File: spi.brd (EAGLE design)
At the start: 40.3 x 33 mm, 7 parts, among them IC2 25AA080SN, IC3 25AA080P, X1 2510-

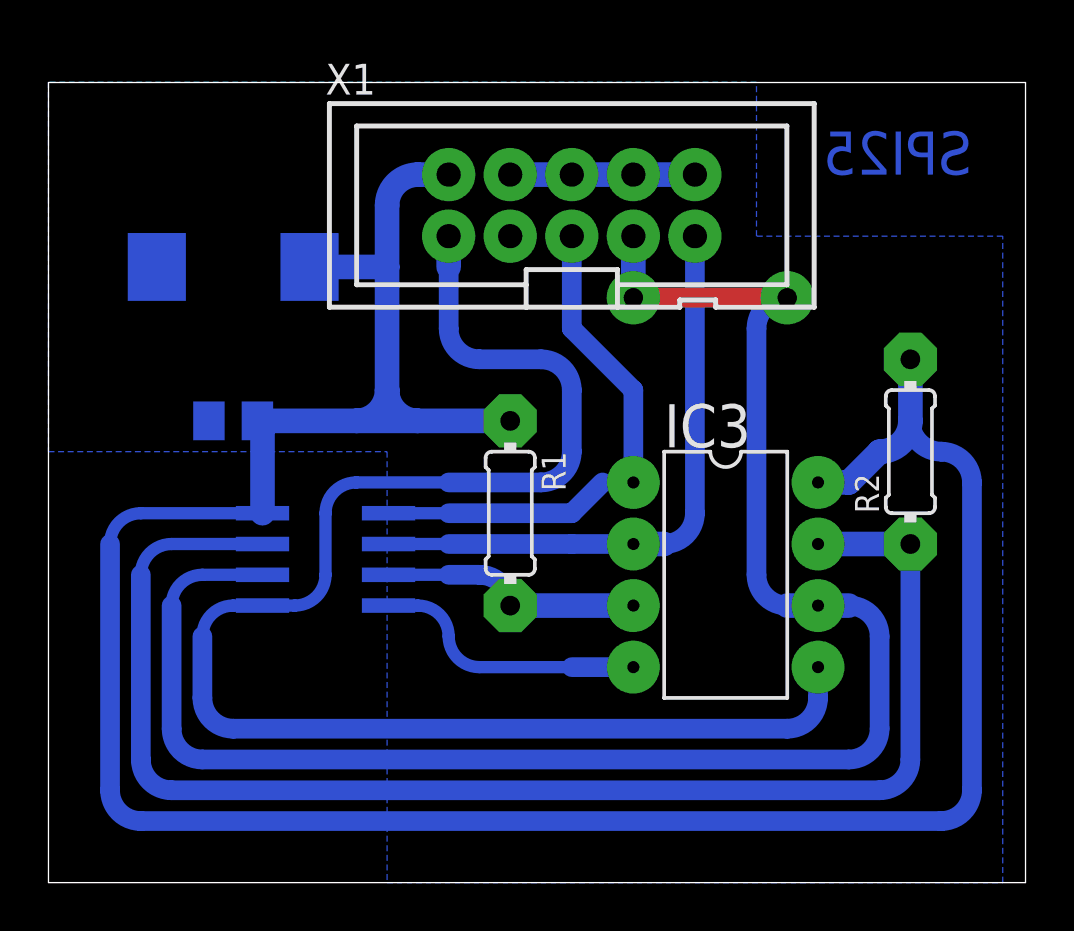
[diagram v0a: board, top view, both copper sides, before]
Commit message: 25 серия использует so-8 в 200 mil
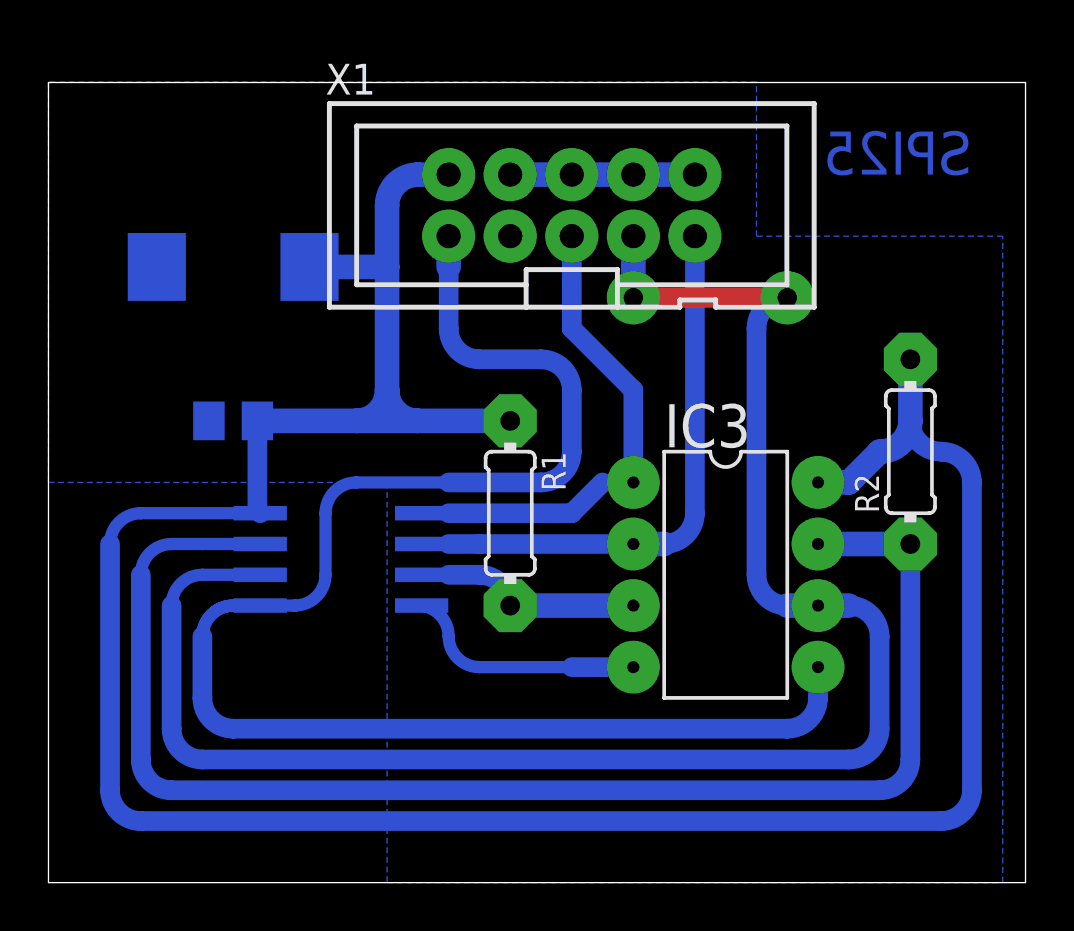
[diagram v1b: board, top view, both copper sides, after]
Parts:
- IC2: value 25AA080SN -> 25; device microchip:SO-08 -> microchip:SO-08M
- moved IC2 0.63 mm to (15.9, 29.8)
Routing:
- net SI: track 62.6 -> 64.4 mm
- net WP: track 11.3 -> 9.92 mm
- net CS: track 21.8 -> 20.5 mm
- net GND: track 18.8 -> 17.6 mm
